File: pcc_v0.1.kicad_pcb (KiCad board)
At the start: 2 copper layers, 190.3 x 121.7 mm, 60 parts, among them J1 Conn_01x02_Socket, J2 Conn_01x04_Socket, J3 Conn_01x02_Socket, J4 Conn_02x14_Counter_Clockwise, J6 Conn_01x04_Socket, J7 Conn_01x04_Socket, J8 Conn_01x02_Socket, J9 Conn_01x02_Socket, K1 G9KB-1A_DC12, K3 PCN-112D3MHZ_000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

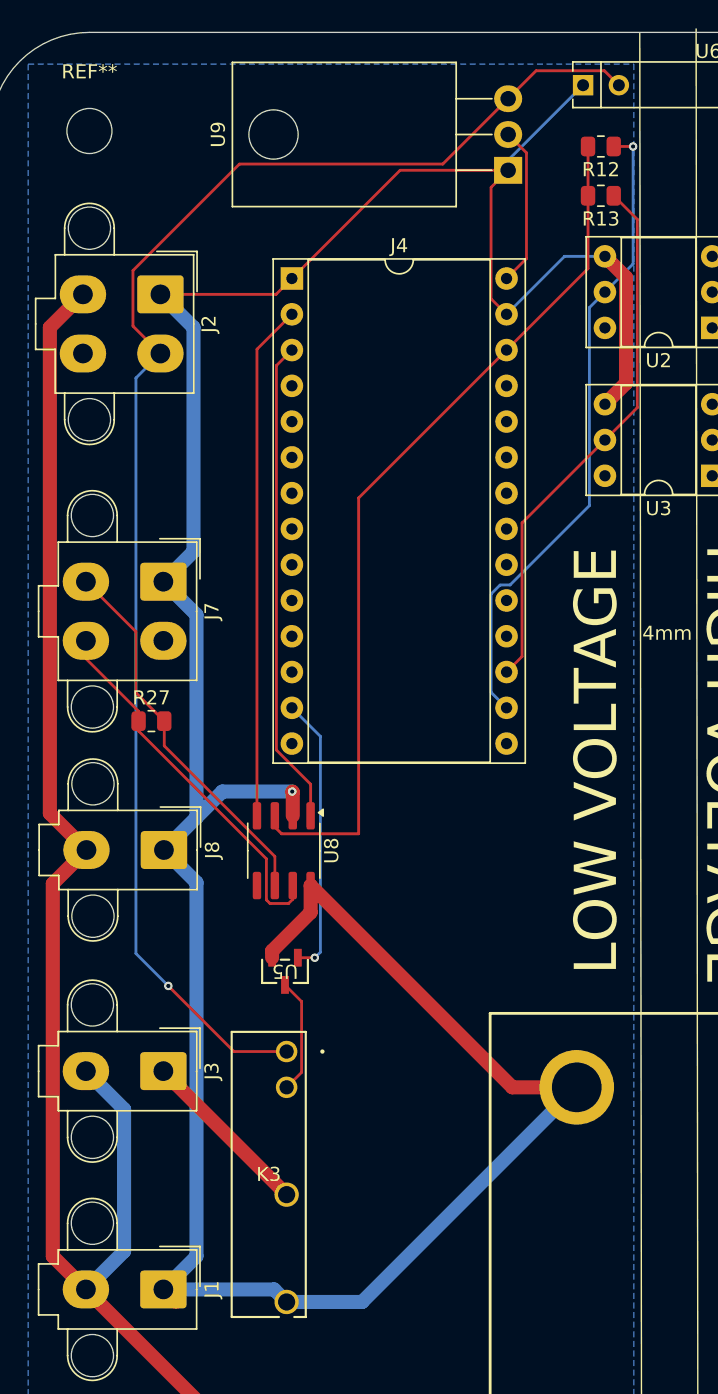
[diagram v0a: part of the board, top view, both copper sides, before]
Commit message: can tranceiver filtering stuff
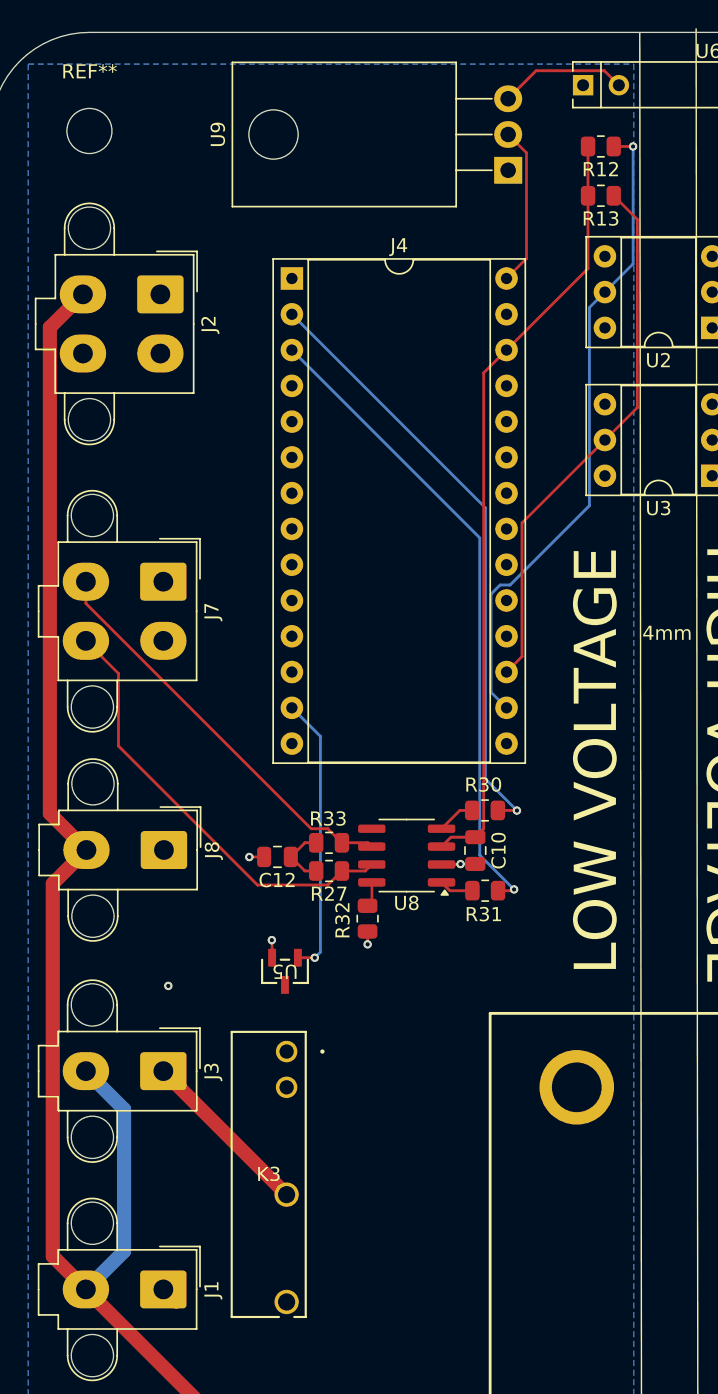
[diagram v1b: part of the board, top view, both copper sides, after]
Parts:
- added C10: 100nF, Capacitor_SMD:C_0805_2012Metric, F.Cu at (88.8, 88.8)
- added C12: 4.7nF, Capacitor_SMD:C_0805_2012Metric, F.Cu at (74.7, 89.3)
- added R30: 10, Resistor_SMD:R_0805_2012Metric, F.Cu at (89.4, 86.0)
- added R31: 10, Resistor_SMD:R_0805_2012Metric, F.Cu at (89.5, 91.7)
- added R32: 10, Resistor_SMD:R_0805_2012Metric, F.Cu at (81.1, 93.7)
- added R33: 60, Resistor_SMD:R_0805_2012Metric, F.Cu at (78.4, 88.3)
- R27: value 120 -> 60
- moved R27 16.5 mm to (78.4, 90.3), turned to 180 degrees
- moved U8 8.73 mm to (83.9, 89.2), turned to 180 degrees
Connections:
- R27 pad 2: CANL -> Net-(C12-Pad1)
- U8 pad 1: CANTX -> Net-(U8-D)
- U8 pad 4: CANRX -> Net-(U8-R)
- U8 pad 8: GLV- -> Net-(U8-Rs)
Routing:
- net GLV-: track 222.2 -> 6.90 mm, vias 1 -> 4
- net +12V: track 104.4 -> 9.11 mm
- net CANTX: track 34.5 -> 46.0 mm, vias 0 -> 1
- net Net-(U5-S): track 8.20 -> 0.00 mm
- net +3.3V: track 62.5 -> 55.0 mm
- net CANRX: track 36.6 -> 43.2 mm, vias 0 -> 1
- net Net-(C12-Pad1): track 0.00 -> 4.43 mm
- net CANH: track 26.8 -> 31.1 mm
- net Net-(U8-R): track 0.00 -> 2.71 mm
- net Net-(U8-D): track 0.00 -> 2.43 mm
- net CANL: track 27.1 -> 29.0 mm
- net Net-(U8-Rs): track 0.00 -> 1.78 mm

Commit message: added discharge relay
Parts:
- removed J9: Conn_01x02_Socket, Connector_Molex:Molex_Mini-Fit_Jr_5566-02A2_2x01_P4.20mm_Vertical
- added K2: DBR71210, discharge relay:DBR71210, F.Cu at (154.6, 152.2)
- moved C10 10.2 mm to (87.2, 78.7)
- moved C12 10.2 mm to (73.2, 79.2)
- moved K1 10.2 mm to (94.4, 135.6)
- moved R27 10.2 mm to (76.8, 80.2)
- moved R28 10.2 mm to (143.3, 136.0)
- moved R33 10.2 mm to (76.8, 78.2)
- moved C8 10.2 mm to (140.3, 53.2)
- moved R1 10.2 mm to (174.2, 30.0)
- moved R16 10.2 mm to (127.5, 27.4)
- moved R17 10.2 mm to (121.8, 42.2)
- moved REF** 10.2 mm to (59.8, 27.6)
- moved U6 10.2 mm to (94.8, 24.4)
- moved C1 10.2 mm to (140.1, 35.1)
- moved C2 10.2 mm to (136.6, 35.2)
- moved C3 10.2 mm to (133.3, 35.1)
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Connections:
- R28 pad 1: GNDS -> TS-
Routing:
- net GNDS: track 372.2 -> 186.0 mm
- net TS+: track 16.7 -> 166.6 mm
- net TS-: track 22.0 -> 115.4 mm
- net +12V: track 9.11 -> 98.4 mm
- net Shutdown_in: track 137.9 -> 195.4 mm
- net Vin_Accu: track 104.4 -> 155.1 mm
- net Net-(U5-S): track 0.00 -> 8.20 mm
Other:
- board size 190.3 x 121.7 mm -> 190.3 x 141.7 mm

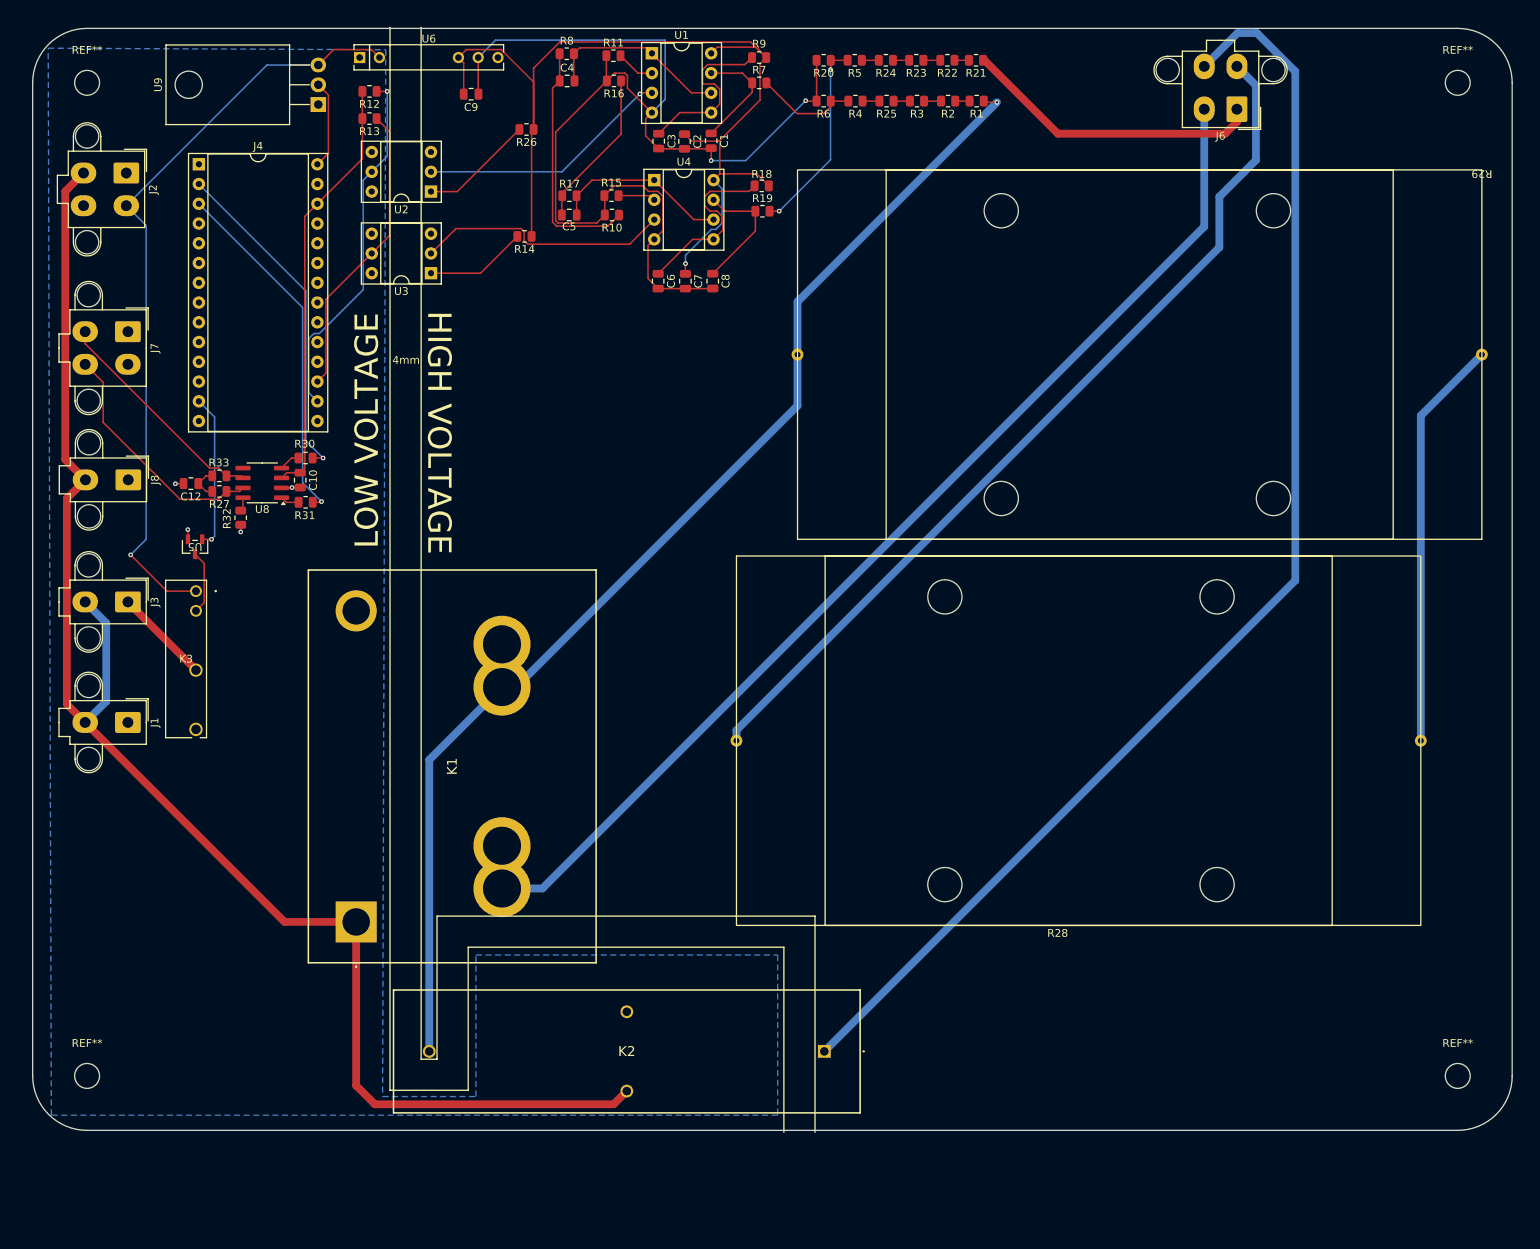
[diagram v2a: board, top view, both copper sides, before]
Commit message: fixed text placement
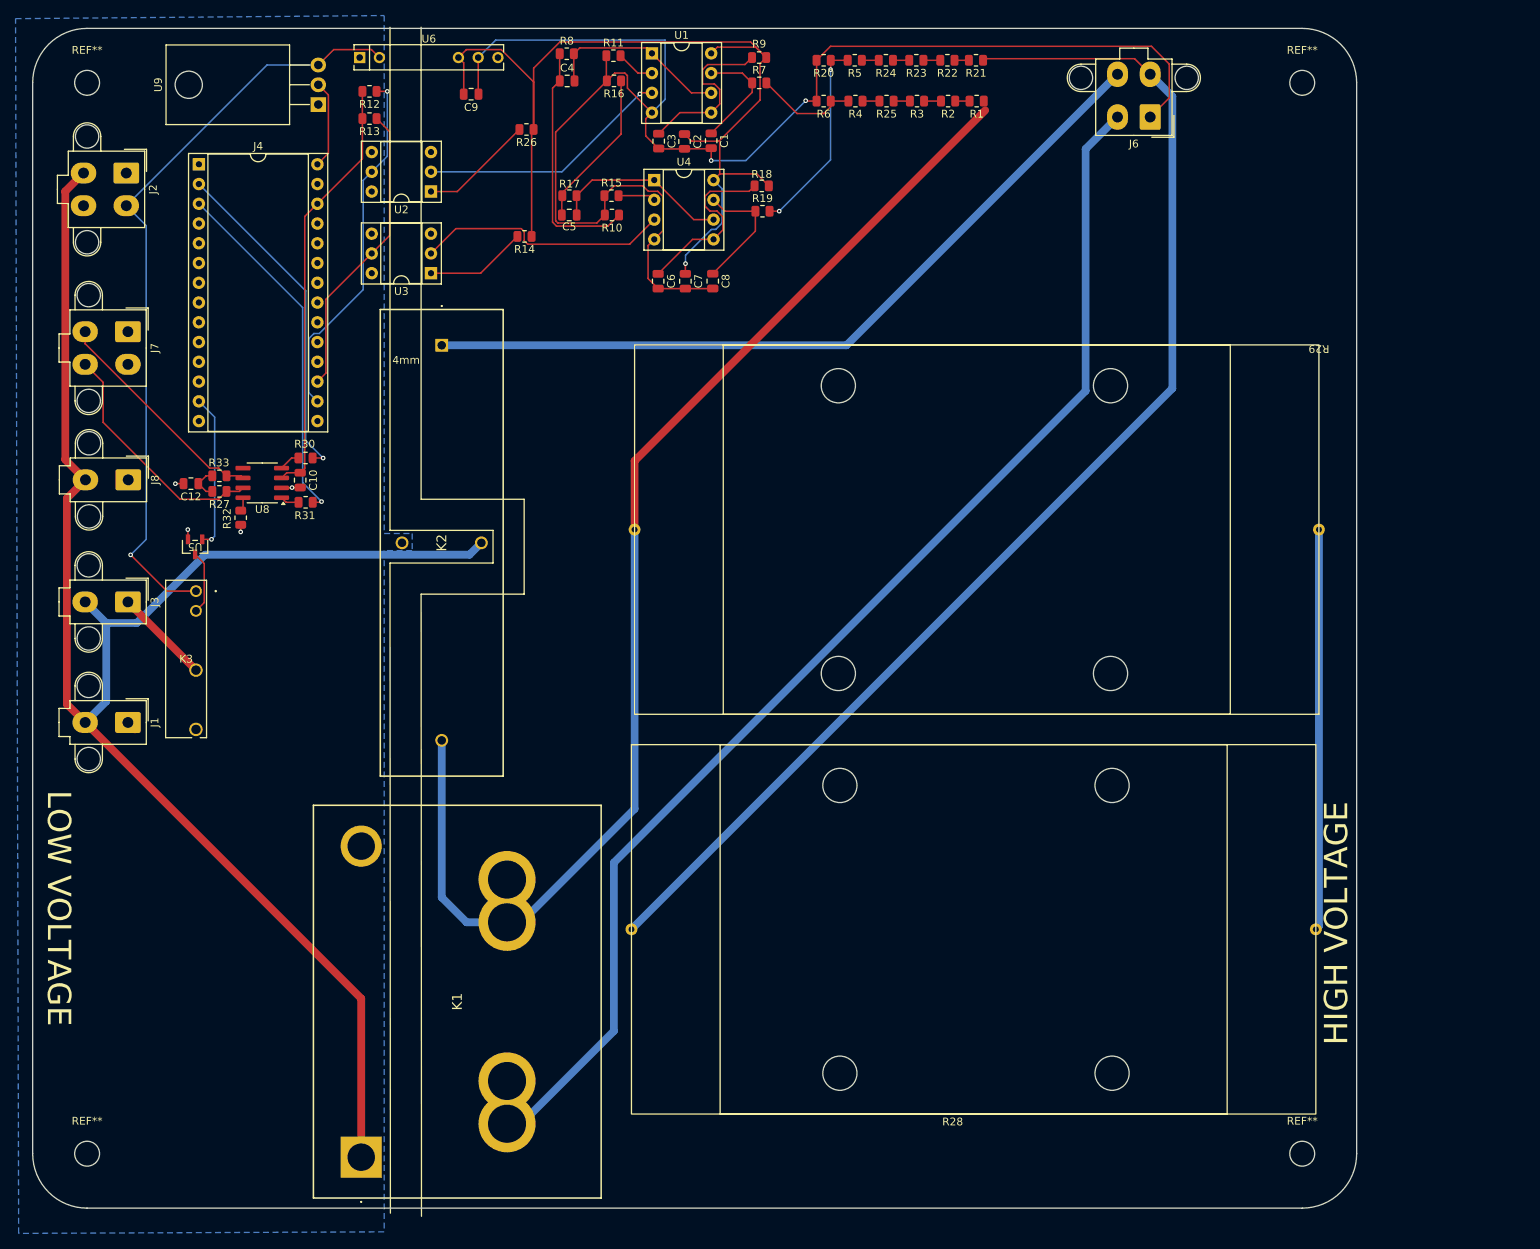
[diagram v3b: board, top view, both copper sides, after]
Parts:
- moved K2 103.3 mm to (105.4, 61.4), turned to -90 degrees
- moved R29 30.7 mm to (218.2, 61.4)
- moved K1 30.3 mm to (95.0, 165.8)
- moved R28 27.8 mm to (129.8, 160.2)
- moved REF** 22.4 mm to (216.1, 165.4)
- moved REF** 20.0 mm to (216.1, 27.6)
- moved J6 11.2 mm to (196.5, 32.0)
- moved REF** 10.0 mm to (59.8, 165.4)
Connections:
- R21 pad 1: GNDS -> TS-
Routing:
- net TS+: track 166.6 -> 101.3 mm
- net TS-: track 115.4 -> 162.3 mm
- net B+_in: track 140.7 -> 163.0 mm
- net Shutdown_in: track 195.4 -> 215.5 mm
- net GNDS: track 186.0 -> 202.3 mm
- net Vin_Accu: track 155.1 -> 160.9 mm, vias 1 -> 0
- net Net-(R28-Pad2): track 52.9 -> 51.6 mm
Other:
- board size 190.3 x 141.7 mm -> 170.3 x 151.7 mm

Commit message: generated bom
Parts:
- removed J1: Conn_01x02_Socket, Connector_Molex:Molex_Mini-Fit_Jr_5566-02A2_2x01_P4.20mm_Vertical
- moved J8 58.1 mm to (64.0, 136.8)
- moved J7 58.1 mm to (64.0, 117.8)
- moved J3 58.1 mm to (64.0, 152.5)
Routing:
- net IR+_GND: track 12.4 -> 53.4 mm
- net CANH: track 31.1 -> 57.2 mm
- net CANL: track 29.0 -> 49.8 mm
- net Shutdown_in: track 215.5 -> 207.5 mm
- net +12V: track 98.4 -> 94.6 mm, vias 1 -> 0
- net GLV-: track 6.90 -> 5.64 mm
